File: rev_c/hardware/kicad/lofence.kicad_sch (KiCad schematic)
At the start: 61 parts, among them J1 Fence+, J2 Fence-, J3 ISP, J4 DEBUG RN, J5 DEBUG LED, J6 DEBUG MCU, J7 868, SW1 RESET, U1 Opamp_Dual_Generic, U3 ATmega328PB-AU, U4 RN2483, U5 MCP125x, Y1 32768 Hz

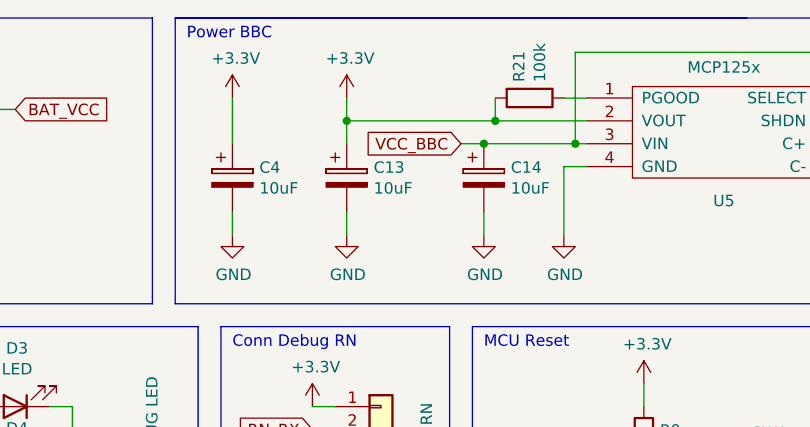
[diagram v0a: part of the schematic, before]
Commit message: fix battery power
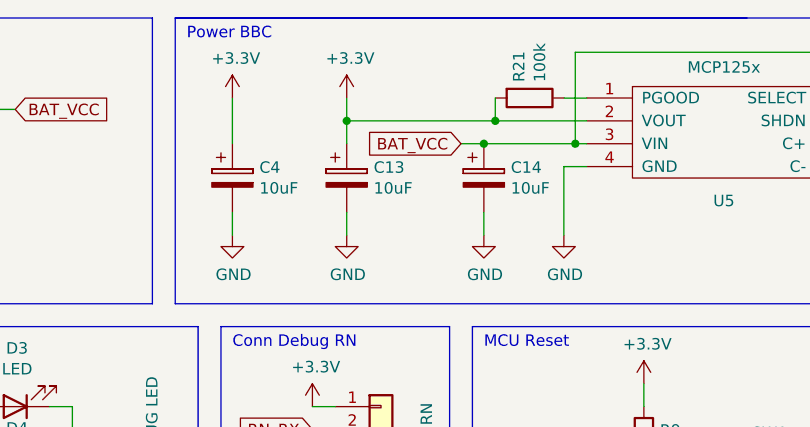
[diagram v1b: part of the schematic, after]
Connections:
- net VCC_BBC is gone; now on net BAT_VCC: C14.1, U5.3 (VIN), U5.7 (SHDN), U5.8 (SELECT)
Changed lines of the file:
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@@
     )
   )
-  (global_label "VCC_BBC" (shape input) (at 91.44 27.94 180) (fields_autoplaced)
+  (global_label "BAT_VCC" (shape input) (at 91.44 27.94 180) (fields_autoplaced)
     (effects (font (size 1.27 1.27)) (justify right))
-    (property "Intersheet References" "${INTERSHEET_REFS}" (id 0) (at -46.99 0 0)
-      (effects (font (size 1.27 1.27)) hide)
+    (property "Intersheet References" "${INTERSHEET_REFS}" (id 0) (at 81.1934 27.8606 0)
+      (effects (font (size 1.27 1.27)) (justify right) hide)
     )
   )
